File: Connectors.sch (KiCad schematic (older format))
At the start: 1 part

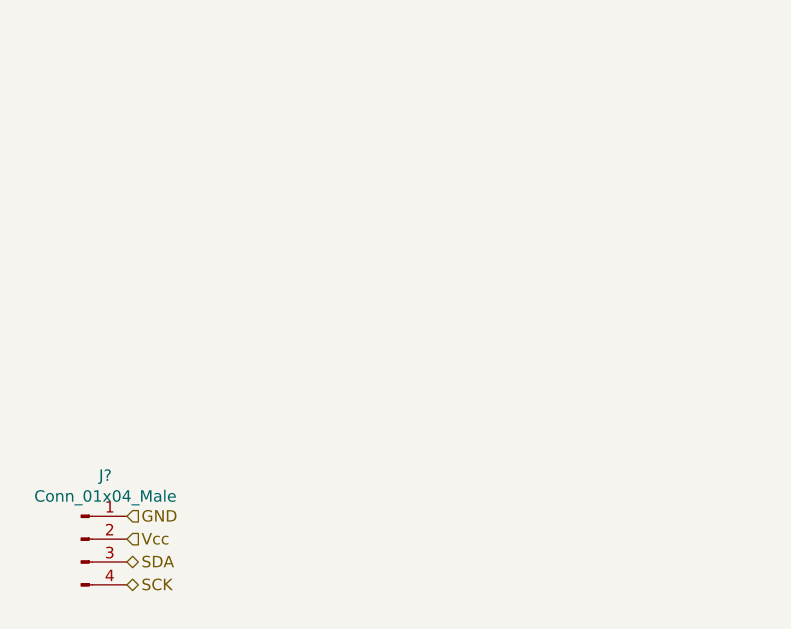
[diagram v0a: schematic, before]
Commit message: Placed symbols in connectors sheet.
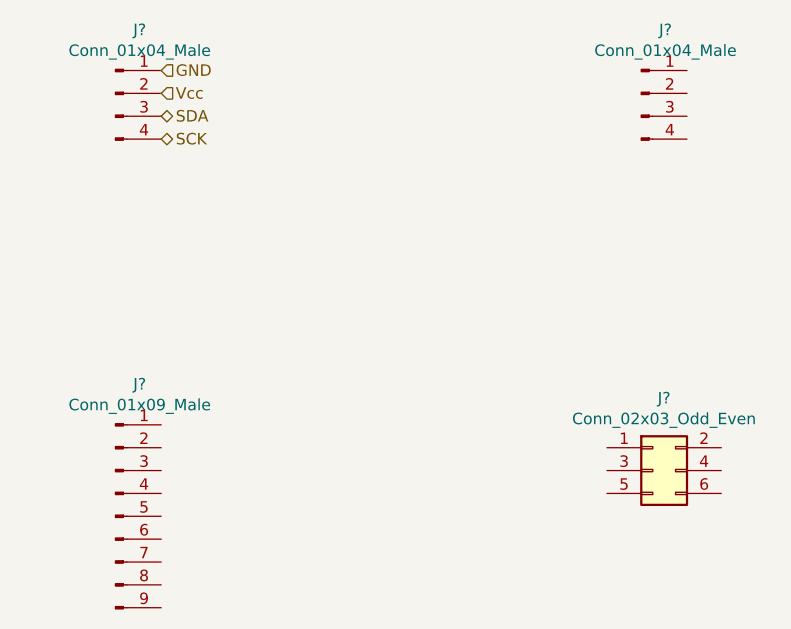
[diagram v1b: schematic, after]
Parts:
- added J?: Conn_01x09_Male, symbol Connector:Conn_01x09_Male
- added J?: Conn_01x04_Male, symbol Connector:Conn_01x04_Male
- added J?: Conn_02x03_Odd_Even, symbol Connector_Generic:Conn_02x03_Odd_Even
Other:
- moved on the sheet: J?
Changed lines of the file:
@@
 L Connector:Conn_01x04_Male J?
 U 1 1 5B7FE24C
-P 4850 3500
-F 0 "J?" H 4956 3778 50  0000 C CNN
-F 1 "Conn_01x04_Male" H 4956 3687 50  0000 C CNN
-F 2 "" H 4850 3500 50  0001 C CNN
-F 3 "~" H 4850 3500 50  0001 C CNN
-	1    4850 3500
+P 5000 1550
+F 0 "J?" H 5106 1828 50  0000 C CNN
+F 1 "Conn_01x04_Male" H 5106 1737 50  0000 C CNN
+F 2 "" H 5000 1550 50  0001 C CNN
+F 3 "~" H 5000 1550 50  0001 C CNN
+	1    5000 1550
 	1    0    0    -1
 $EndComp
-Text HLabel 5050 3400 2    50   Input ~ 0
+Text HLabel 5200 1450 2    50   Input ~ 0
 GND
-Text HLabel 5050 3500 2    50   Input ~ 0
+Text HLabel 5200 1550 2    50   Input ~ 0
 Vcc
-Text HLabel 5050 3600 2    50   BiDi ~ 0
+Text HLabel 5200 1650 2    50   BiDi ~ 0
 SDA
-Text HLabel 5050 3700 2    50   BiDi ~ 0
+Text HLabel 5200 1750 2    50   BiDi ~ 0
 SCK
+$Comp
+L Connector:Conn_01x09_Male J?
+U 1 1 5B7FEDEF
+P 5000 3400
+F 0 "J?" H 5106 3978 50  0000 C CNN
+F 1 "Conn_01x09_Male" H 5106 3887 50  0000 C CNN
+F 2 "" H 5000 3400 50  0001 C CNN
+F 3 "~" H 5000 3400 50  0001 C CNN
+	1    5000 3400
+	1    0    0    -1
+$EndComp
+$Comp
+L Connector:Conn_01x04_Male J?
+U 1 1 5B7FEE85
+P 7300 1550
+F 0 "J?" H 7406 1828 50  0000 C CNN
+F 1 "Conn_01x04_Male" H 7406 1737 50  0000 C CNN
+F 2 "" H 7300 1550 50  0001 C CNN
+F 3 "~" H 7300 1550 50  0001 C CNN
+	1    7300 1550
+	1    0    0    -1
+$EndComp
+$Comp
+L Connector_Generic:Conn_02x03_Odd_Even J?
+U 1 1 5B7FEF30
+P 7350 3200
+F 0 "J?" H 7400 3517 50  0000 C CNN
+F 1 "Conn_02x03_Odd_Even" H 7400 3426 50  0000 C CNN
+F 2 "" H 7350 3200 50  0001 C CNN
+F 3 "~" H 7350 3200 50  0001 C CNN
+	1    7350 3200
+	1    0    0    -1
+$EndComp
 $EndSCHEMATC
